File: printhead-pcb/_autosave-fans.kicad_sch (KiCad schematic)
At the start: 14 parts, among them J2 Fan_12/5V_Regelung, J4 FAN0, J5 FAN1, J6 FAN2, J7 FAN4, Q1 DTC143E, Q2 DTC143E, Q4 DTC143E, Q5 DTC143E, U2 EMC2302-2-AIZL-TR

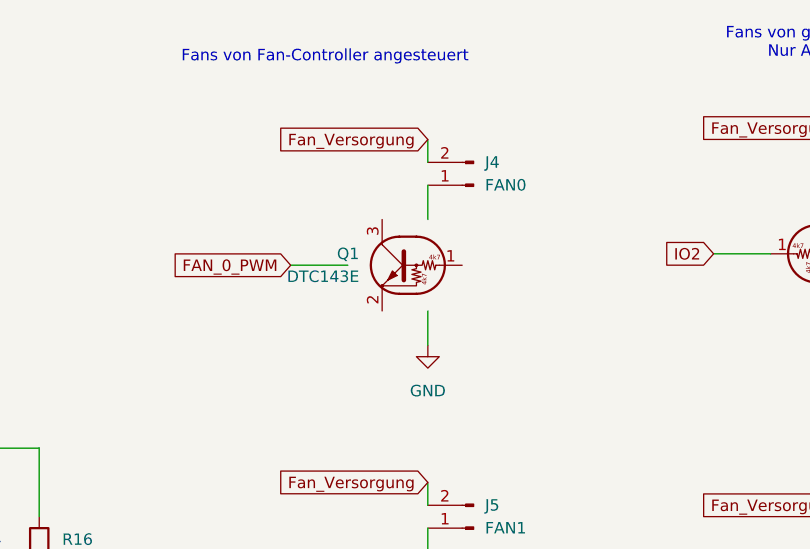
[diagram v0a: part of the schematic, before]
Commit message: second module repositioned, now working on the routing
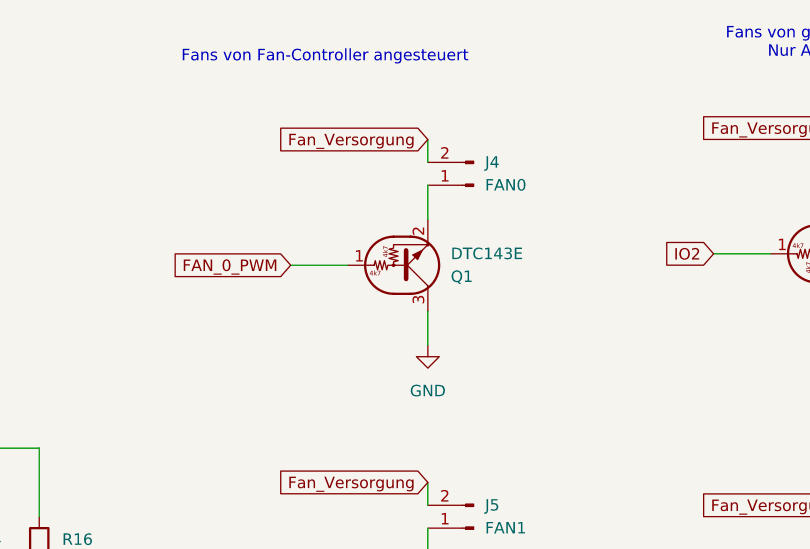
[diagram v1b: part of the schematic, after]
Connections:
- net FAN_0_PWM: now also Q1.1 (B)
- net GND: now also Q1.3 (C)
- net at J4.1 (Pin_1): now also Q1.2 (E)
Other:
- moved on the sheet: Q1
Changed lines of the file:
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@@
 		(lib_id "Transistor_BJT:DTC143E")
 		(at 182.88 77.47 0)
-		(mirror y)
+		(mirror x)
 		(unit 1)
 		(exclude_from_sim no)
@@
 		(dnp no)
 		(property "Reference" "Q1"
-			(at 177.8 76.1999 0)
+			(at 187.96 78.7401 0)
 			(effects
 				(font
@@
 		)
 		(property "Value" "DTC143E"
-			(at 177.8 78.7399 0)
+			(at 187.96 76.2001 0)
 			(effects
 				(font
